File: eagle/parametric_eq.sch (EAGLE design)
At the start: 41 parts, among them IC1 TL072P, IC2 TL072P

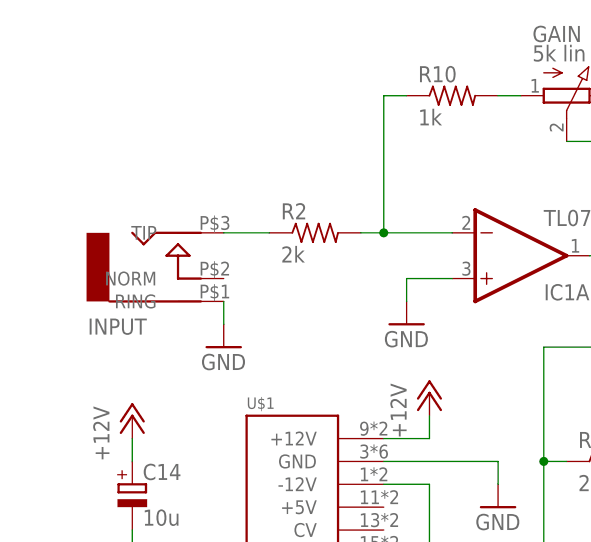
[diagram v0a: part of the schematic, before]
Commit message: dc reject cap
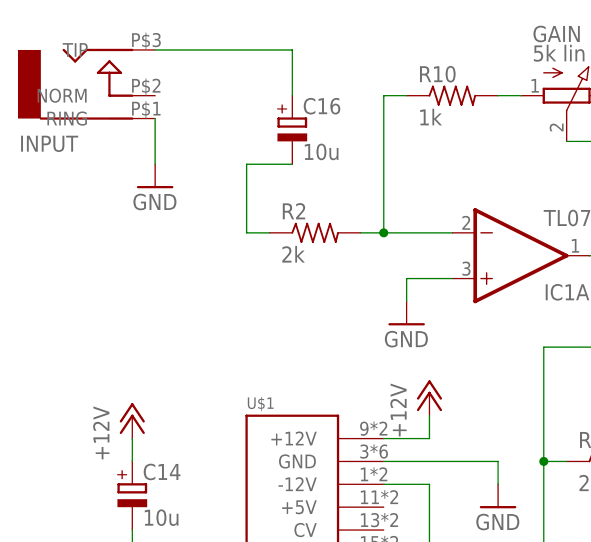
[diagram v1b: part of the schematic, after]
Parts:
- added C16: 10u, rcl:CPOL-EUB45181A
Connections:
- new net N$24: C16.-, R2.1
- net N$9: now also C16.+; no longer R2.1
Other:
- moved on the sheet: INPUT
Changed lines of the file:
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@@
 <part name="C15" library="rcl" deviceset="CPOL-EU" device="B45181A" value="10u"/>
 <part name="GND8" library="supply1" deviceset="GND" device=""/>
+<part name="C16" library="rcl" deviceset="CPOL-EU" device="B45181A" value="10u"/>
 </parts>
 <sheets>
@@
 <instance part="OUT" gate="G$1" x="182.88" y="43.18" rot="R180"/>
 <instance part="GND12" gate="1" x="175.26" y="33.02"/>
-<instance part="INPUT" gate="G$1" x="-5.08" y="71.12" rot="MR180"/>
-<instance part="GND7" gate="1" x="2.54" y="63.5"/>
+<instance part="INPUT" gate="G$1" x="-12.7" y="91.44" rot="MR180"/>
+<instance part="GND7" gate="1" x="-5.08" y="81.28"/>
 <instance part="LOWFREQ" gate="/1" x="58.42" y="30.48" rot="MR180"/>
 <instance part="LOWFREQ" gate="/2" x="71.12" y="30.48" rot="MR180"/>
@@
 <instance part="C15" gate="G$1" x="-7.62" y="35.56"/>
 <instance part="GND8" gate="1" x="0" y="38.1"/>
+<instance part="C16" gate="G$1" x="10.16" y="88.9"/>
 </instances>
 <busses>
@@
 <pinref part="INPUT" gate="G$1" pin="RING"/>
 <pinref part="GND7" gate="1" pin="GND"/>
-<wire x1="2.54" y1="66.04" x2="2.54" y2="68.58" width="0.1524" layer="91"/>
+<wire x1="-5.08" y1="83.82" x2="-5.08" y2="88.9" width="0.1524" layer="91"/>
 </segment>
 <segment>
@@
 <net name="N$9" class="0">
 <segment>
+<pinref part="INPUT" gate="G$1" pin="TIP"/>
+<pinref part="C16" gate="G$1" pin="+"/>
+<wire x1="-5.08" y1="96.52" x2="10.16" y2="96.52" width="0.1524" layer="91"/>
+<wire x1="10.16" y1="96.52" x2="10.16" y2="91.44" width="0.1524" layer="91"/>
+</segment>
+</net>
+<net name="N$24" class="0">
+<segment>
+<pinref part="C16" gate="G$1" pin="-"/>
+<wire x1="10.16" y1="83.82" x2="5.08" y2="83.82" width="0.1524" layer="91"/>
+<wire x1="5.08" y1="83.82" x2="5.08" y2="76.2" width="0.1524" layer="91"/>
 <pinref part="R2" gate="G$1" pin="1"/>
-<pinref part="INPUT" gate="G$1" pin="TIP"/>
-<wire x1="2.54" y1="76.2" x2="7.62" y2="76.2" width="0.1524" layer="91"/>
-</segment>
-</net>
+<wire x1="5.08" y1="76.2" x2="7.62" y2="76.2" width="0.1524" layer="91"/>
+</segment>
+</net>

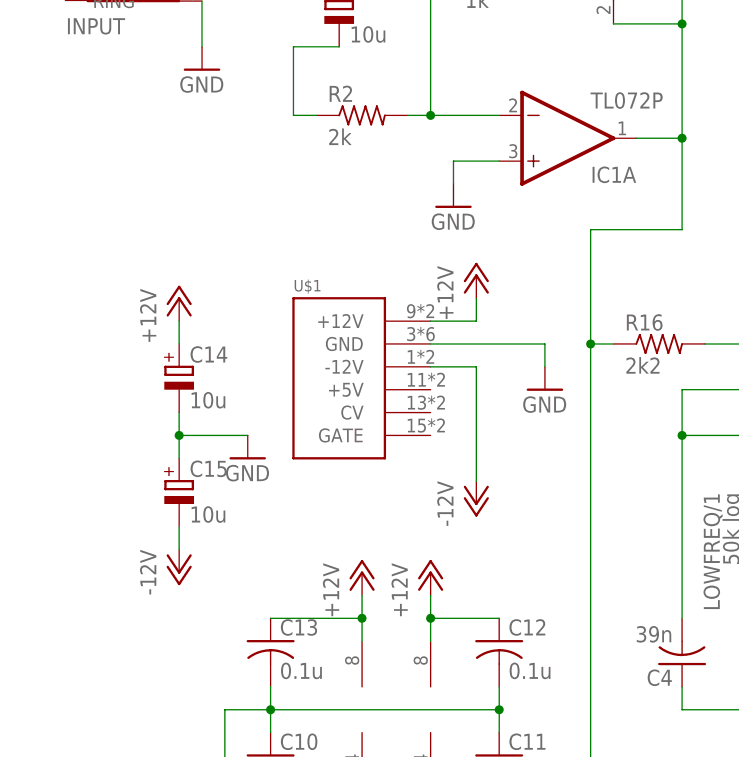
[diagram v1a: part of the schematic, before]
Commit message: ferrite beads and thick traces
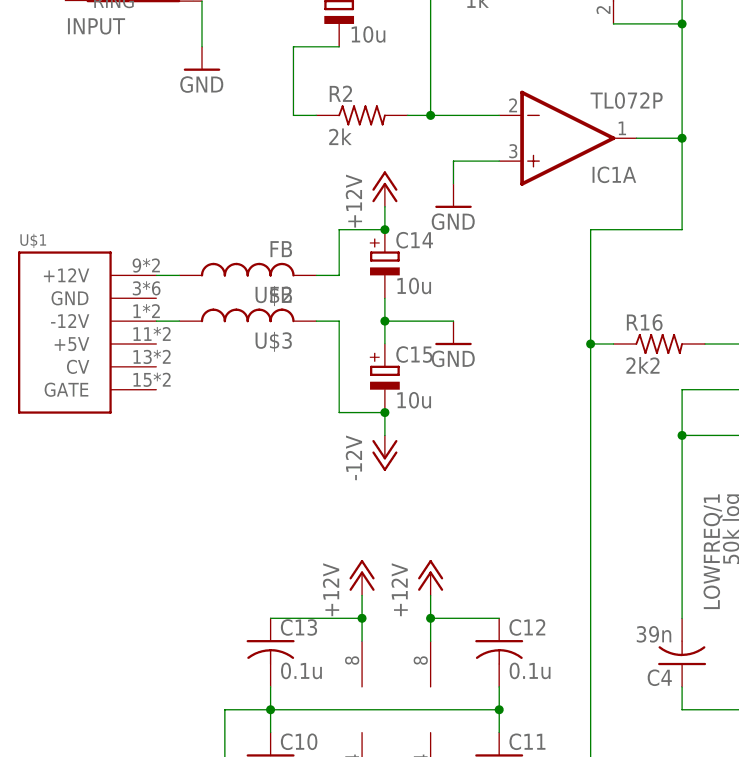
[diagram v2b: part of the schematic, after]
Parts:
- added U$2, U$3: FB, adafruit:FB
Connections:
- new net N$25: U$1.+12V, U$2.1
- new net N$26: U$1.-12V, U$3.1
- net +12V: now also U$2.2; no longer U$1.+12V
- net -12V: now also U$3.2; no longer U$1.-12V
- net GND: no longer U$1.GND
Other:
- moved on the sheet: C14, C15, U$1

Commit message: 7mm 15n cap, new schematic png
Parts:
- C7: device rcl:C-US050-050X075 -> rcl:C-US075-032X103
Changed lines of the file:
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@@
 <grid distance="0.1" unitdist="inch" unit="inch" style="lines" multiple="1" display="no" altdistance="0.01" altunitdist="inch" altunit="inch"/>
 <layers>
-<layer number="1" name="Top" color="4" fill="1" visible="no" active="no"/>
-<layer number="16" name="Bottom" color="1" fill="1" visible="no" active="no"/>
-<layer number="17" name="Pads" color="2" fill="1" visible="no" active="no"/>
-<layer number="18" name="Vias" color="2" fill="1" visible="no" active="no"/>
-<layer number="19" name="Unrouted" color="6" fill="1" visible="no" active="no"/>
-<layer number="20" name="Dimension" color="15" fill="1" visible="no" active="no"/>
-<layer number="21" name="tPlace" color="7" fill="1" visible="no" active="no"/>
-<layer number="22" name="bPlace" color="7" fill="1" visible="no" active="no"/>
-<layer number="23" name="tOrigins" color="15" fill="1" visible="no" active="no"/>
-<layer number="24" name="bOrigins" color="15" fill="1" visible="no" active="no"/>
-<layer number="25" name="tNames" color="7" fill="1" visible="no" active="no"/>
-<layer number="26" name="bNames" color="7" fill="1" visible="no" active="no"/>
-<layer number="27" name="tValues" color="7" fill="1" visible="no" active="no"/>
-<layer number="28" name="bValues" color="7" fill="1" visible="no" active="no"/>
+<layer number="1" name="Top" color="4" fill="1" visible="yes" active="no"/>
+<layer number="16" name="Bottom" color="1" fill="1" visible="yes" active="no"/>
+<layer number="17" name="Pads" color="2" fill="1" visible="yes" active="no"/>
+<layer number="18" name="Vias" color="2" fill="1" visible="yes" active="no"/>
+<layer number="19" name="Unrouted" color="6" fill="1" visible="yes" active="no"/>
+<layer number="20" name="Dimension" color="15" fill="1" visible="yes" active="no"/>
+<layer number="21" name="tPlace" color="7" fill="1" visible="yes" active="no"/>
+<layer number="22" name="bPlace" color="7" fill="1" visible="yes" active="no"/>
+<layer number="23" name="tOrigins" color="15" fill="1" visible="yes" active="no"/>
+<layer number="24" name="bOrigins" color="15" fill="1" visible="yes" active="no"/>
+<layer number="25" name="tNames" color="7" fill="1" visible="yes" active="no"/>
+<layer number="26" name="bNames" color="7" fill="1" visible="yes" active="no"/>
+<layer number="27" name="tValues" color="7" fill="1" visible="yes" active="no"/>
+<layer number="28" name="bValues" color="7" fill="1" visible="yes" active="no"/>
 <layer number="29" name="tStop" color="7" fill="3" visible="no" active="no"/>
 <layer number="30" name="bStop" color="7" fill="6" visible="no" active="no"/>
@@
 <layer number="35" name="tGlue" color="7" fill="4" visible="no" active="no"/>
 <layer number="36" name="bGlue" color="7" fill="5" visible="no" active="no"/>
-<layer number="37" name="tTest" color="7" fill="1" visible="no" active="no"/>
-<layer number="38" name="bTest" color="7" fill="1" visible="no" active="no"/>
+<layer number="37" name="tTest" color="7" fill="1" visible="yes" active="no"/>
+<layer number="38" name="bTest" color="7" fill="1" visible="yes" active="no"/>
 <layer number="39" name="tKeepout" color="4" fill="11" visible="no" active="no"/>
 <layer number="40" name="bKeepout" color="1" fill="11" visible="no" active="no"/>
@@
 <layer number="44" name="Drills" color="7" fill="1" visible="no" active="no"/>
 <layer number="45" name="Holes" color="7" fill="1" visible="no" active="no"/>
-<layer number="46" name="Milling" color="3" fill="1" visible="no" active="no"/>
-<layer number="47" name="Measures" color="7" fill="1" visible="no" active="no"/>
-<layer number="48" name="Document" color="7" fill="1" visible="no" active="no"/>
-<layer number="49" name="Reference" color="7" fill="1" visible="no" active="no"/>
-<layer number="50" name="dxf" color="7" fill="1" visible="no" active="no"/>
-<layer number="51" name="tDocu" color="7" fill="1" visible="no" active="no"/>
-<layer number="52" name="bDocu" color="7" fill="1" visible="no" active="no"/>
-<layer number="53" name="tGND_GNDA" color="7" fill="9" visible="no" active="no"/>
-<layer number="54" name="bGND_GNDA" color="1" fill="9" visible="no" active="no"/>
-<layer number="56" name="wert" color="7" fill="1" visible="no" active="no"/>
-<layer number="57" name="tCAD" color="7" fill="1" visible="no" active="no"/>
+<layer number="46" name="Milling" color="3" fill="1" visible="yes" active="no"/>
+<layer number="47" name="Measures" color="7" fill="1" visible="yes" active="no"/>
+<layer number="48" name="Document" color="7" fill="1" visible="yes" active="no"/>
+<layer number="49" name="Reference" color="7" fill="1" visible="yes" active="no"/>
+<layer number="50" name="dxf" color="7" fill="1" visible="yes" active="no"/>
+<layer number="51" name="tDocu" color="7" fill="1" visible="yes" active="no"/>
+<layer number="52" name="bDocu" color="7" fill="1" visible="yes" active="no"/>
+<layer number="53" name="tGND_GNDA" color="7" fill="9" visible="yes" active="no"/>
+<layer number="54" name="bGND_GNDA" color="1" fill="9" visible="yes" active="no"/>
+<layer number="56" name="wert" color="7" fill="1" visible="yes" active="no"/>
+<layer number="57" name="tCAD" color="7" fill="1" visible="yes" active="no"/>
 <layer number="90" name="Modules" color="5" fill="1" visible="yes" active="yes"/>
 <layer number="91" name="Nets" color="2" fill="1" visible="yes" active="yes"/>
@@
 <part name="C5" library="rcl" deviceset="C-US" device="050-050X075" value="100n"/>
 <part name="C6" library="rcl" deviceset="C-US" device="050-050X075" value="5n6"/>
-<part name="C7" library="rcl" deviceset="C-US" device="050-050X075" value="15n"/>
+<part name="C7" library="rcl" deviceset="C-US" device="075-032X103" value="15n"/>
 <part name="C8" library="rcl" deviceset="C-US" device="050-050X075" value="1n8"/>
 <part name="C9" library="rcl" deviceset="C-US" device="050-050X075" value="4n7"/>
